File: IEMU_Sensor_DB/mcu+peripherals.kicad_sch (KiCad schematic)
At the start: 34 parts, among them J201 Conn_ARM_SWD_TagConnect_TC203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, U201 Ezurio BL54L15, U202 W25N02JWZEIF, U203 LSM6DSV320XTR, U204 MMC5603NJ, Y201 32.768kHz

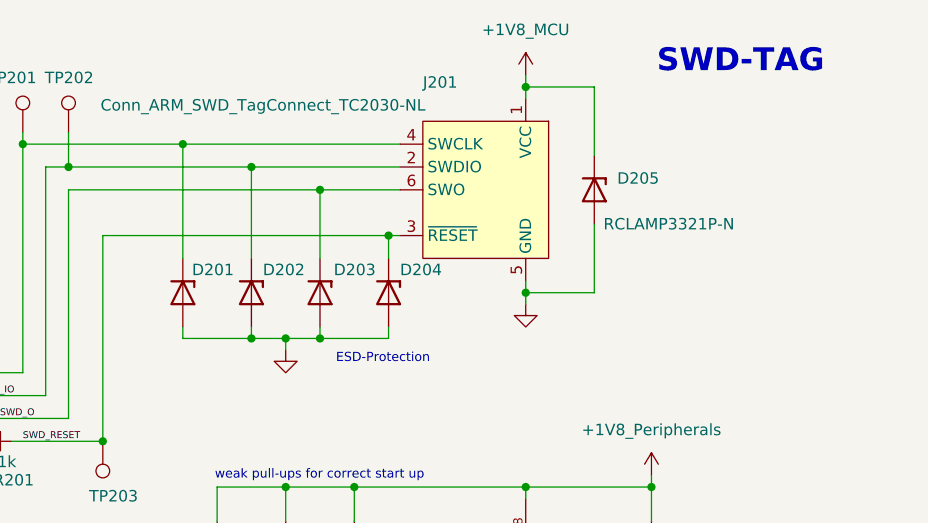
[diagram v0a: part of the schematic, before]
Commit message: finished schematic revision based on TF-review by implementing sensor schematic too
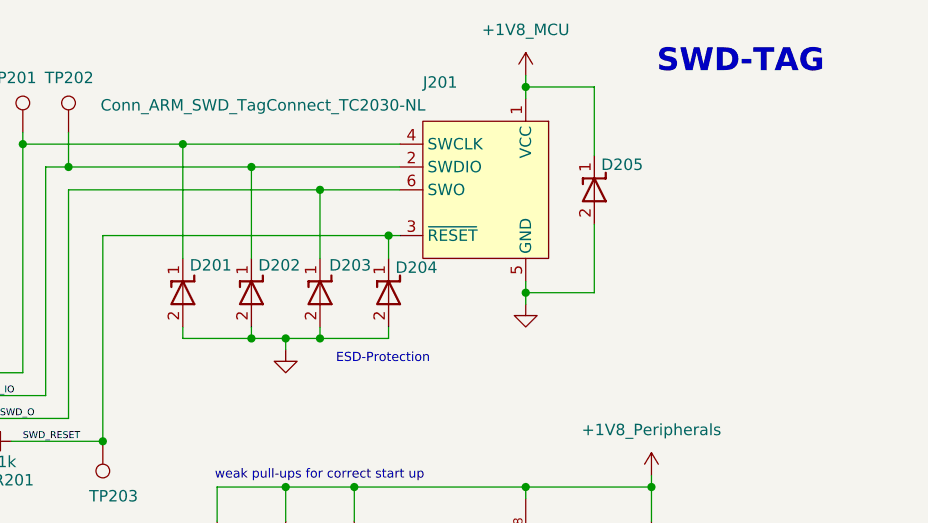
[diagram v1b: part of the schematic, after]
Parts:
- removed D201, D202, D203, D204, D205: RCLAMP3321P-N, Diode_SMD:D_SOD-882, symbol 0_Connectors:RCLAMP3321P-N
- added D201, D202, D203, D204, D205: ESD9L1P8, Diode_SMD:D_SOD-882, symbol 0_Power:ESD9L1P8
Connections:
- net +1V8_MCU: now also D205.1 (I/O)
- net GND: now also D201.2 (GND), D202.2 (GND), D203.2 (GND), D204.2 (GND), D205.2 (GND)
- net SWD_CLK: now also D201.1 (I/O)
- net SWD_IO: now also D202.1 (I/O)
- net SWD_O: now also D203.1 (I/O)
- net SWD_RESET: now also D204.1 (I/O)

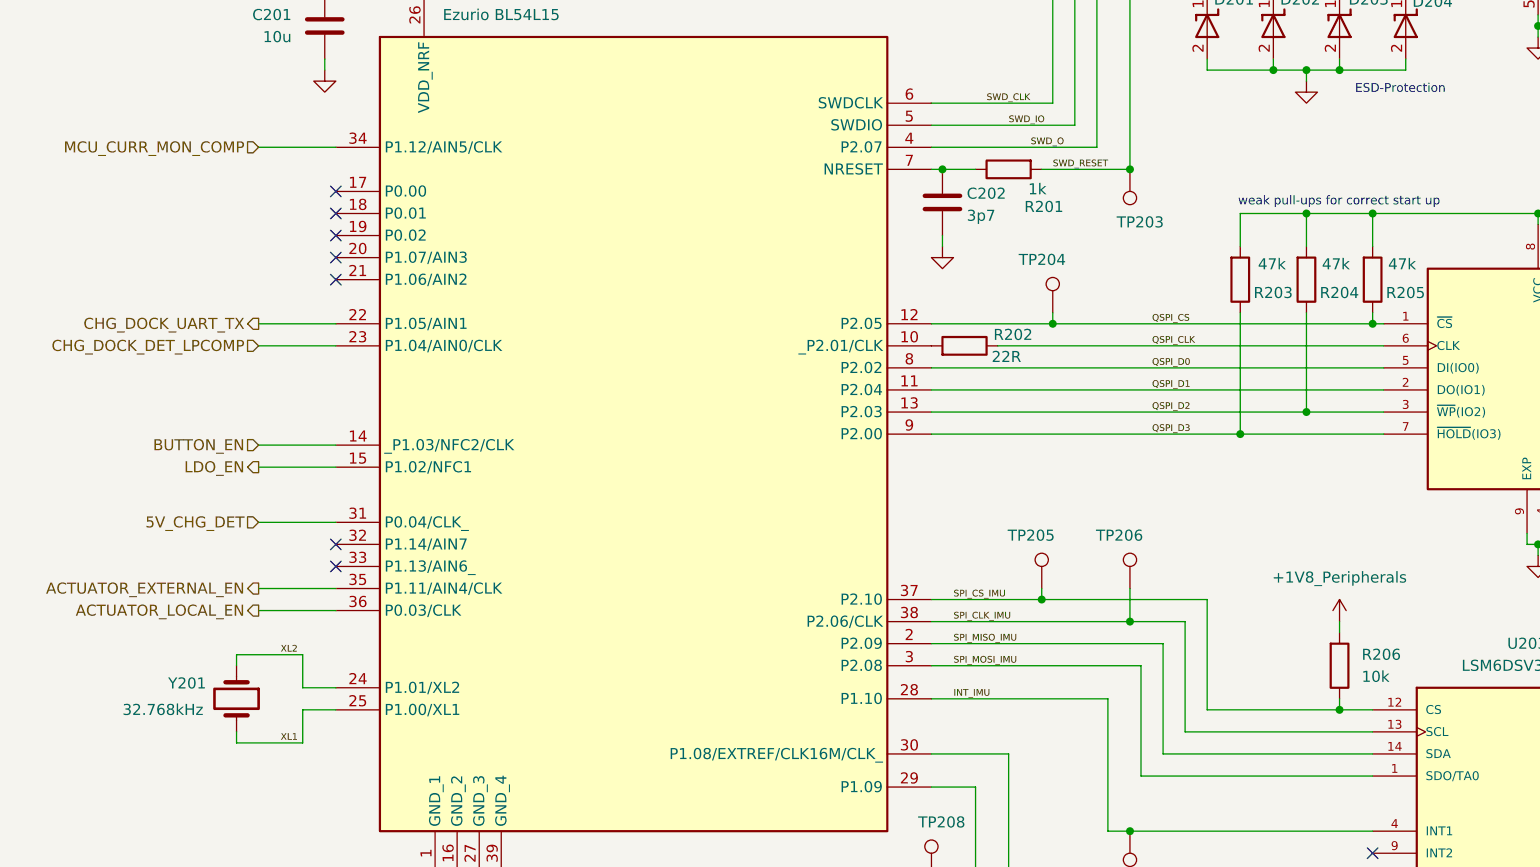
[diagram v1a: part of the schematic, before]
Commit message: created the layout for the sensor (not finished)
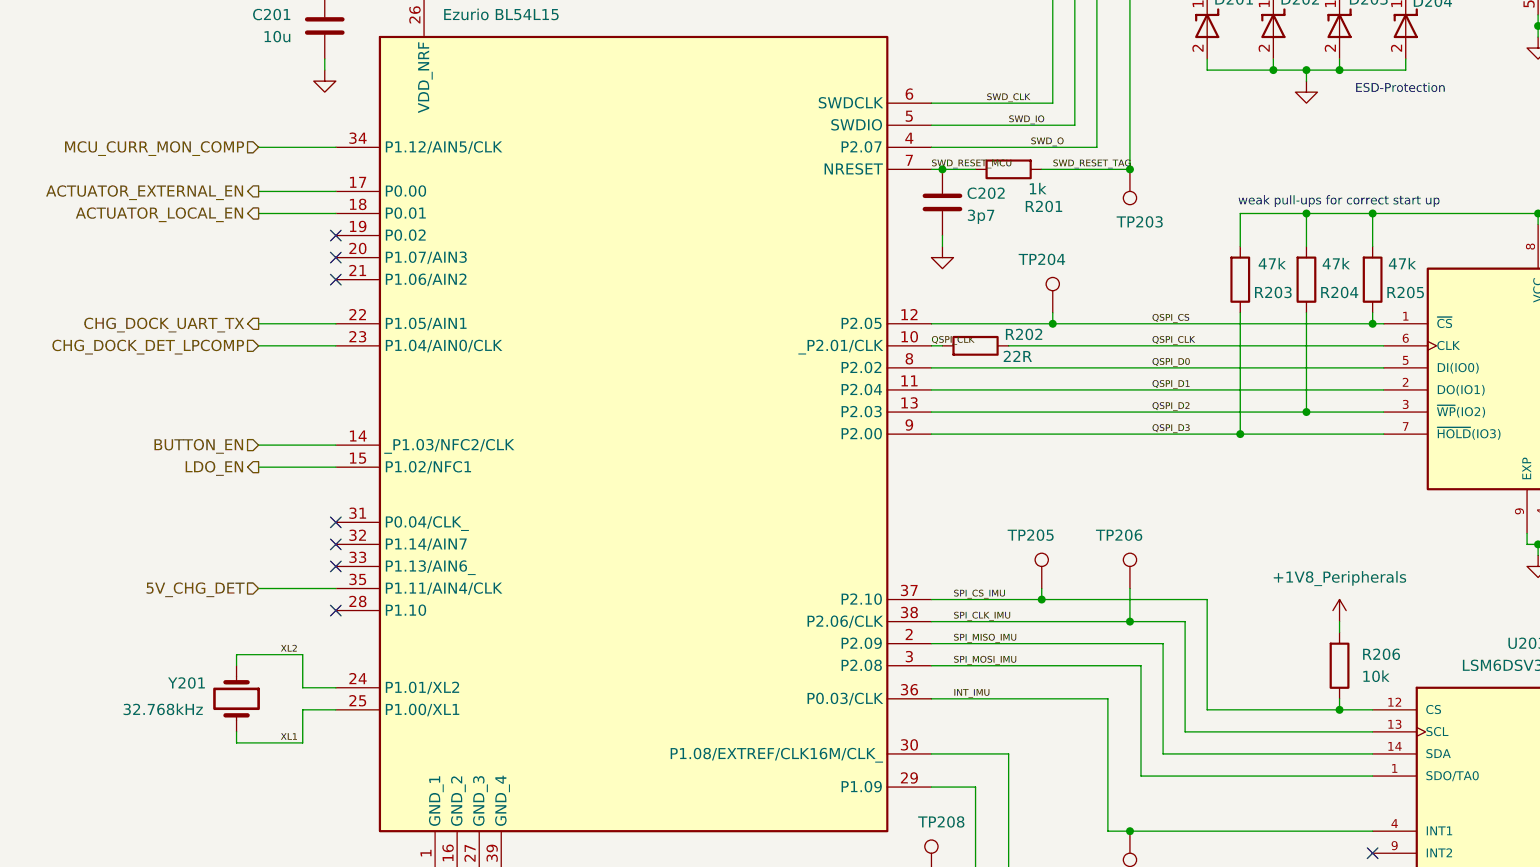
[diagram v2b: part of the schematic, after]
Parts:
- TP201, TP202, TP203, TP204, TP205, TP206, TP207, TP208, TP209: footprint TestPoint:TestPoint_Pad_D2.0mm -> TestPoint:TestPoint_Pad_D1.0mm
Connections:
- net 5V_CHG_DET: now also U201.35 (P1.11/AIN4/CLK); no longer U201.31 (P0.04/CLK_)
- net ACTUATOR_EXTERNAL_EN: now also U201.17 (P0.00); no longer U201.35 (P1.11/AIN4/CLK)
- net ACTUATOR_LOCAL_EN: now also U201.18 (P0.01); no longer U201.36 (P0.03/CLK)
- net INT_IMU: now also U201.36 (P0.03/CLK); no longer U201.28 (P1.10)
- net QSPI_CLK: now also R202.1, U201.10 (_P2.01/CLK)
- net SWD_RESET_MCU: now reaches C202.1, R201.2, U201.7 (NRESET)
- net SWD_RESET renamed SWD_RESET_TAG
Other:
- moved on the sheet: R202
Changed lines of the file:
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@@
 	)
 	(no_connect
-		(at 48.26 106.68)
-	)
-	(no_connect
 		(at 167.64 142.24)
 	)
@@
 	)
 	(no_connect
-		(at 48.26 68.58)
-	)
-	(no_connect
 		(at 48.26 73.66)
 	)
 	(no_connect
-		(at 48.26 66.04)
+		(at 48.26 71.12)
 	)
 	(no_connect
-		(at 48.26 71.12)
+		(at 48.26 104.14)
 	)
 	(no_connect
@@
 		(at 48.26 109.22)
 	)
+	(no_connect
+		(at 48.26 106.68)
+	)
+	(no_connect
+		(at 48.26 114.3)
+	)
 	(wire
 		(pts
@@
 	(wire
 		(pts
+			(xy 118.11 83.82) (xy 116.84 83.82)
+		)
+		(stroke
+			(width 0)
+			(type default)
+		)
+	)
+	(wire
+		(pts
 			(xy 39.37 60.96) (xy 48.26 60.96)
 		)
@@
 	(wire
 		(pts
+			(xy 39.37 68.58) (xy 48.26 68.58)
+		)
+		(stroke
+			(width 0)
+			(type default)
+		)
+	)
+	(wire
+		(pts
 			(xy 135.89 33.02) (xy 133.35 33.02)
 		)
@@
 	(wire
 		(pts
-			(xy 39.37 114.3) (xy 48.26 114.3)
-		)
-		(stroke
-			(width 0)
-			(type default)
-		)
-	)
-	(wire
-		(pts
 			(xy 171.45 52.07) (xy 171.45 50.8)
 		)
@@
 	(wire
 		(pts
-			(xy 124.46 83.82) (xy 168.91 83.82)
+			(xy 125.73 83.82) (xy 168.91 83.82)
 		)
 		(stroke
@@
 	(wire
 		(pts
-			(xy 39.37 104.14) (xy 48.26 104.14)
+			(xy 39.37 111.76) (xy 48.26 111.76)
 		)
 		(stroke
@@
 	(wire
 		(pts
-			(xy 39.37 111.76) (xy 48.26 111.76)
-		)
-		(stroke
-			(width 0)
-			(type default)
-		)
-	)
-	(wire
-		(pts
 			(xy 158.75 186.69) (xy 156.21 186.69)
 		)
@@
 	(wire
 		(pts
+			(xy 39.37 66.04) (xy 48.26 66.04)
+		)
+		(stroke
+			(width 0)
+			(type default)
+		)
+	)
+	(wire
+		(pts
 			(xy 186.69 22.86) (xy 186.69 24.13)
 		)
@@
 		)
 	)
+	(label "SWD_RESET_MCU"
+		(at 116.84 63.5 0)
+		(effects
+			(font
+				(size 0.762 0.762)
+			)
+			(justify left bottom)
+		)
+	)
 	(label "SWD_CLK"
 		(at 123.19 55.88 0)
@@
 		)
 	)
+	(label "QSPI_CLK"
+		(at 116.84 83.82 0)
+		(effects
+			(font
+				(size 0.762 0.762)
+			)
+			(justify left bottom)
+		)
+	)
 	(label "SPI_CLK_IMU"
 		(at 119.38 115.57 0)
@@
 		)
 	)
-	(label "SWD_RESET"
+	(label "SWD_RESET_TAG"
 		(at 130.81 63.5 0)
 		(effects
@@
 		)
 	)
+	(hierarchical_label "ACTUATOR_LOCAL_EN"
+		(shape output)
+		(at 39.37 68.58 180)
+		(effects
+			(font
+				(size 1.27 1.27)
+			)
+			(justify right)
+		)
+	)
 	(hierarchical_label "CHG_DOCK_DET_LPCOMP"
 		(shape input)
@@
 		)
 	)
-	(hierarchical_label "ACTUATOR_EXTERNAL_EN"
-		(shape output)
-		(at 39.37 111.76 180)
-		(effects
-			(font
-				(size 1.27 1.27)
-			)
-			(justify right)
-		)
-	)
 	(hierarchical_label "CHG_DOCK_UART_TX"
 		(shape output)
@@
 	(hierarchical_label "5V_CHG_DET"
 		(shape input)
-		(at 39.37 104.14 180)
+		(at 39.37 111.76 180)
 		(effects
 			(font
@@
 		)
 	)
-	(hierarchical_label "ACTUATOR_LOCAL_EN"
-		(shape output)
-		(at 39.37 114.3 180)
+	(hierarchical_label "I2C_SDA"
+		(shape bidirectional)
+		(at 111.76 148.59 180)
 		(effects
 			(font
 				(size 1.27 1.27)
+				(thickness 0.254)
+				(bold yes)
 			)
 			(justify right)
 		)
 	)
-	(hierarchical_label "I2C_SDA"
-		(shape bidirectional)
-		(at 111.76 148.59 180)
+	(hierarchical_label "ACTUATOR_EXTERNAL_EN"
+		(shape output)
+		(at 39.37 66.04 180)
 		(effects
 			(font
 				(size 1.27 1.27)
-				(thickness 0.254)
-				(bold yes)
 			)
 			(justify right)
@@
 			)
 		)
-		(property "Footprint" "TestPoint:TestPoint_Pad_D2.0mm"
+		(property "Footprint" "TestPoint:TestPoint_Pad_D1.0mm"
 			(at 144.78 63.5 0)
 			(effects
@@
 			)
 		)
-		(property "Footprint" "TestPoint:TestPoint_Pad_D2.0mm"
+		(property "Footprint" "TestPoint:TestPoint_Pad_D1.0mm"
 			(at 144.78 139.7 0)
 			(effects
@@
 			)
 		)
-		(property "Footprint" "TestPoint:TestPoint_Pad_D2.0mm"
+		(property "Footprint" "TestPoint:TestPoint_Pad_D1.0mm"
 			(at 134.62 111.76 0)
 			(effects
@@
 			)
 		)
-		(property "Footprint" "TestPoint:TestPoint_Pad_D2.0mm"
+		(property "Footprint" "TestPoint:TestPoint_Pad_D1.0mm"
 			(at 125.73 29.21 0)
 			(effects
@@
 			)
 		)
-		(property "Footprint" "TestPoint:TestPoint_Pad_D2.0mm"
+		(property "Footprint" "TestPoint:TestPoint_Pad_D1.0mm"
 			(at 124.46 111.76 0)
 			(effects
@@
 			)
 		)
-		(property "Footprint" "TestPoint:TestPoint_Pad_D2.0mm"
+		(property "Footprint" "TestPoint:TestPoint_Pad_D1.0mm"
 			(at 125.73 80.01 0)
 			(effects
@@
 			)
 		)
-		(property "Footprint" "TestPoint:TestPoint_Pad_D2.0mm"
+		(property "Footprint" "TestPoint:TestPoint_Pad_D1.0mm"
 			(at 130.81 29.21 0)
 			(effects
@@
 			)
 		)
-		(property "Footprint" "TestPoint:TestPoint_Pad_D2.0mm"
+		(property "Footprint" "TestPoint:TestPoint_Pad_D1.0mm"
 			(at 121.92 148.59 0)
 			(effects
@@
 			)
 		)
-		(property "Footprint" "TestPoint:TestPoint_Pad_D2.0mm"
+		(property "Footprint" "TestPoint:TestPoint_Pad_D1.0mm"
 			(at 121.92 144.78 0)
 			(effects
@@
 	(symbol
 		(lib_id "0_Passives:R_22")
-		(at 120.65 83.82 90)
+		(at 121.92 83.82 90)
 		(unit 1)
 		(exclude_from_sim no)
@@
 		(dnp no)
 		(property "Reference" "R202"
-			(at 126.238 82.55 90)
+			(at 127.508 82.55 90)
 			(effects
 				(font
@@
 		)
 		(property "Value" "22R"
-			(at 125.476 85.09 90)
+			(at 126.746 85.09 90)
 			(effects
 				(font
@@
 		)
 		(property "Footprint" "Resistor_SMD:R_0603_1608Metric"
-			(at 120.65 85.598 90)
+			(at 121.92 85.598 90)
 			(effects
 				(font
@@
 		)
 		(property "Datasheet" "https://www.royalohm.com/assets/pdf/products/smd/1.pdf"
-			(at 134.112 83.82 0)
+			(at 135.382 83.82 0)
 			(effects
 				(font
@@
 		)
 		(property "Description" "-55℃~+155℃ 100mW 22Ω 75V Thick Film Resistor ±1% ±100ppm/℃ 0603 Chip Resistor - Surface Mount ROHS"
-			(at 126.238 78.232 0)
+			(at 127.508 78.232 0)
 			(effects
 				(font
@@
 		)
 		(property "Manufacturer_Name" "UNI-ROYAL(Uniroyal Elec)"
-			(at 128.778 83.82 0)
+			(at 130.048 83.82 0)
 			(effects
 				(font
@@
 		)
 		(property "Manufacturer_Part_Number" "0603WAF220JT5E"
-			(at 131.572 83.058 0)
+			(at 132.842 83.058 0)
 			(effects
 				(font
@@
 		)
 		(property "Distributor Link 1" "https://www.mouser.de/ProductDetail/Royalohm/0603WAF220JT5E?qs=e8oIoAS2J1QaFtl9BkMMvg%3D%3D"
-			(at 130.81 81.026 0)
+			(at 132.08 81.026 0)
 			(effects
 				(font
@@
 		)
 		(property "Distributor Link 2" ""
-			(at 120.65 83.82 0)
+			(at 121.92 83.82 0)
 			(effects
 				(font
@@
 		)
 		(property "LCSC" "C23345"
-			(at 140.462 81.026 0)
+			(at 141.732 81.026 0)
 			(effects
 				(font
@@
 		)
 		(property "Distributer Link 1" ""
-			(at 120.65 83.82 90)
+			(at 121.92 83.82 90)
 			(effects
 				(font
@@
 		)
 		(property "Manufactuer_Name" ""
-			(at 120.65 83.82 90)
+			(at 121.92 83.82 90)
 			(effects
 				(font

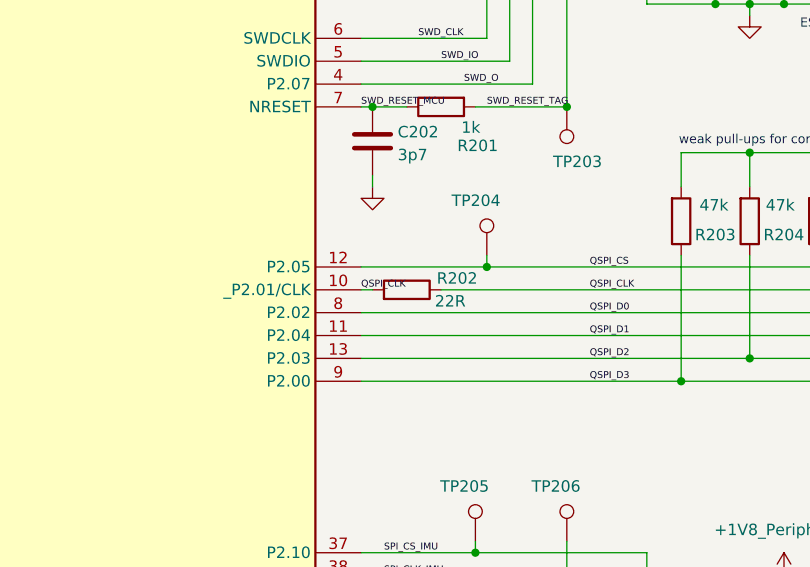
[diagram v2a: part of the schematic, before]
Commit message: finished layout for sensor
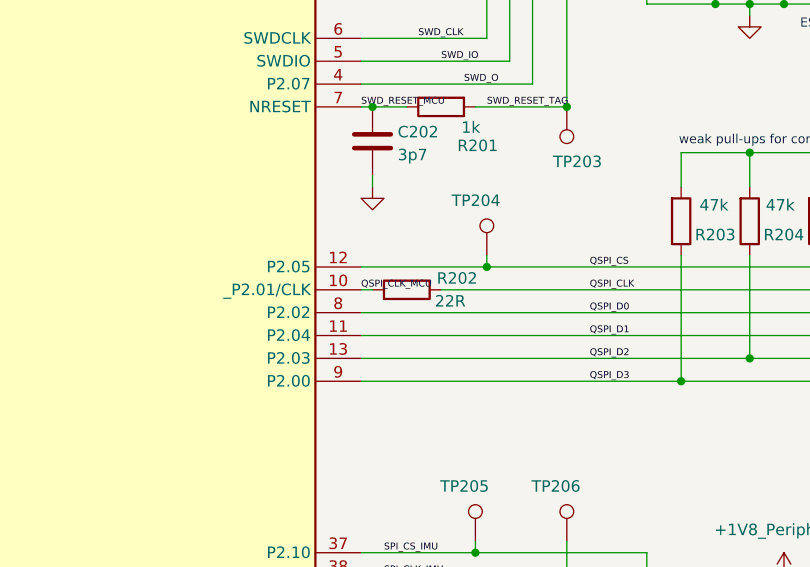
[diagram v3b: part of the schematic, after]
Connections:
- net QSPI_CLK: no longer R202.1, U201.10 (_P2.01/CLK)
- new net QSPI_CLK_MCU: R202.1, U201.10 (_P2.01/CLK)
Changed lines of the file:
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@@
 		)
 	)
-	(label "QSPI_CLK"
+	(label "QSPI_CLK_MCU"
 		(at 116.84 83.82 0)
 		(effects
